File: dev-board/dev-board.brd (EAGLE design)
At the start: 49.2 x 64.8 mm, 43 parts, among them J1 12401832E402A, U1 STM32F103RET6, U2 AT24C64BN-10SU-2.7, U3 FT232RL, U4 MCP2551, U5 LM1117IMP-3.3, X1 8MHz

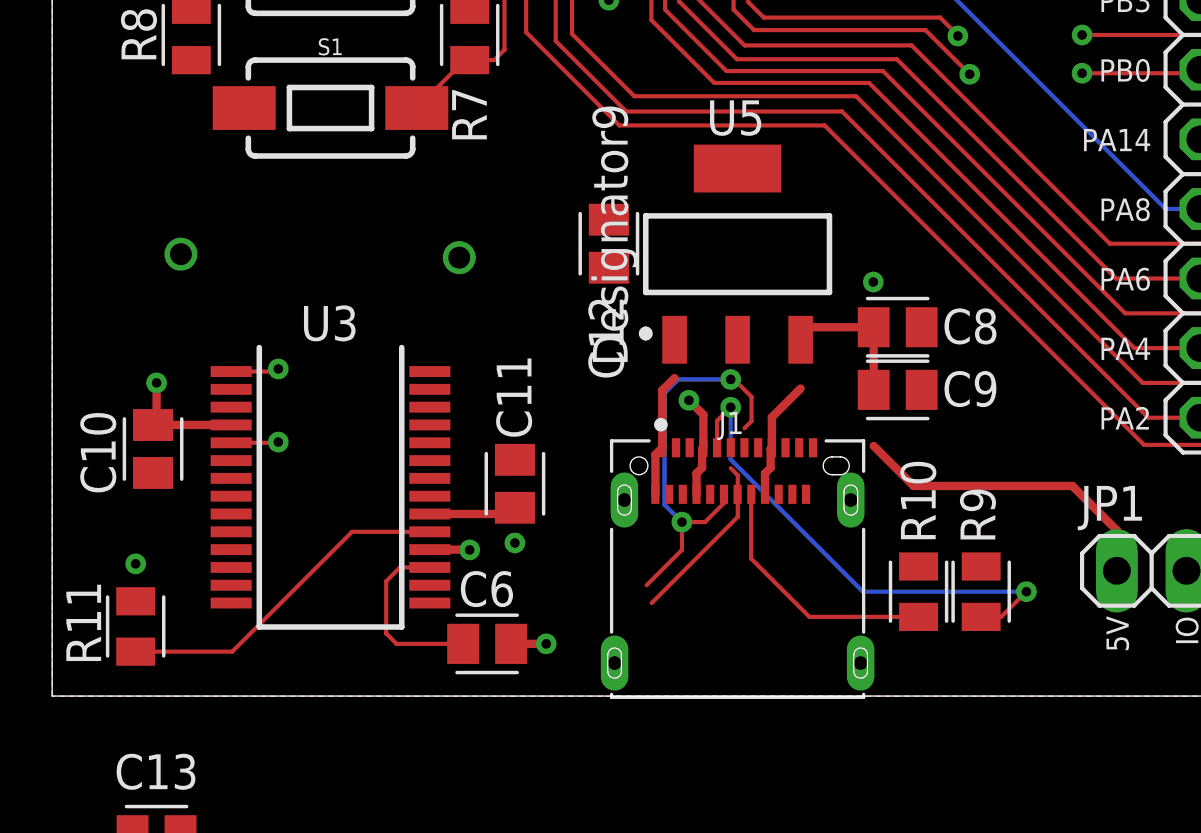
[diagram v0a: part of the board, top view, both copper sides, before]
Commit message: Redesign of dev-board USB connector area
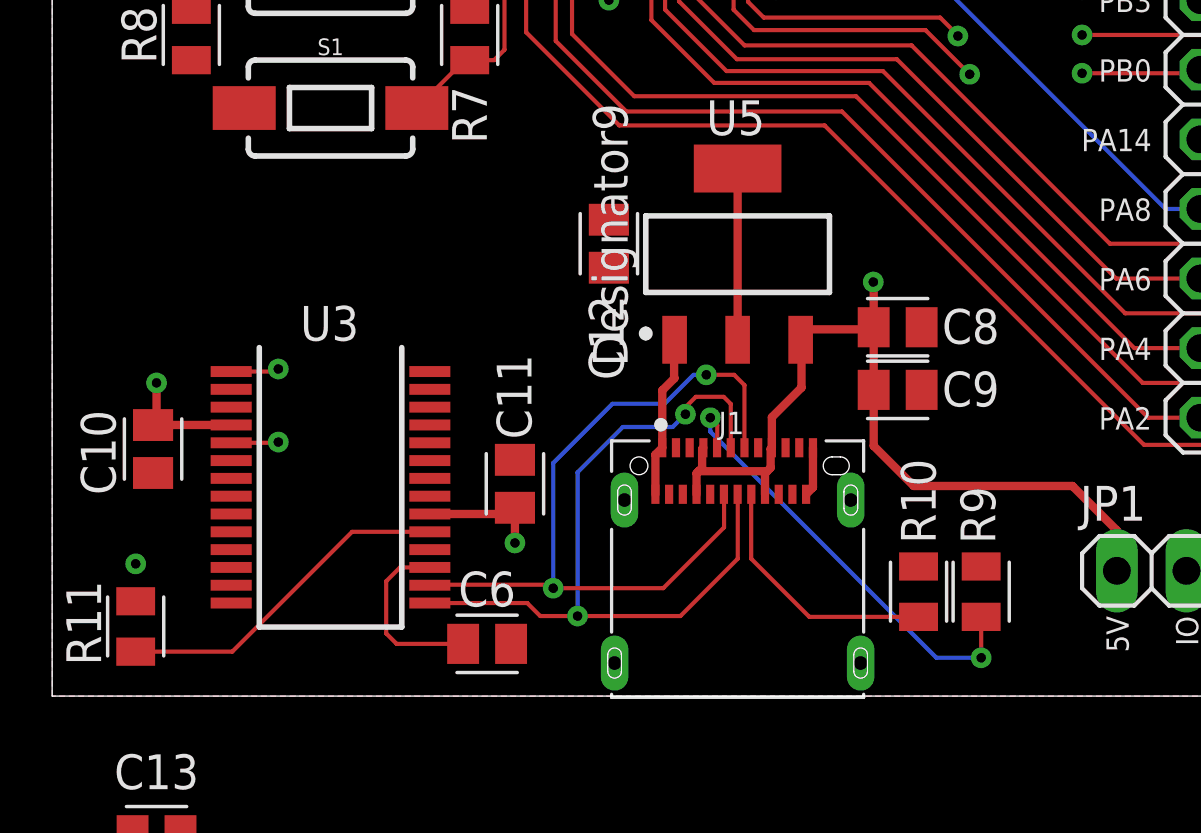
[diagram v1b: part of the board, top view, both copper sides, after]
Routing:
- net USBDP: track 6.34 -> 28.5 mm, vias 0 -> 2
- net USBDM: track 14.8 -> 28.3 mm
- net +5V: track 110.4 -> 117.6 mm, vias 5 -> 4
- net +3V3: track 24.7 -> 31.0 mm
- net N$13: track 18.4 -> 16.5 mm
- net GND: track 9.12 -> 9.60 mm, vias 8 -> 4

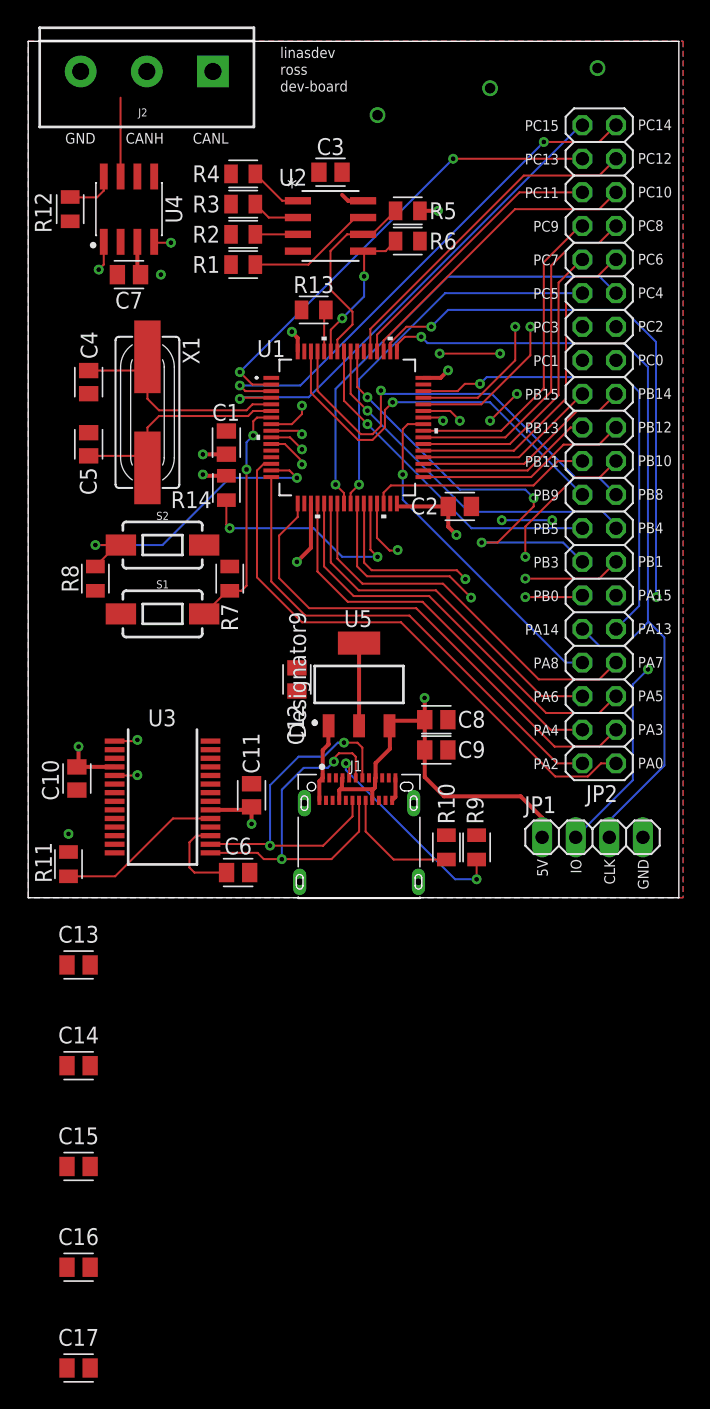
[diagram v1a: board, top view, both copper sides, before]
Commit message: Fix stm32 decoupling caps in dev-board pcb design
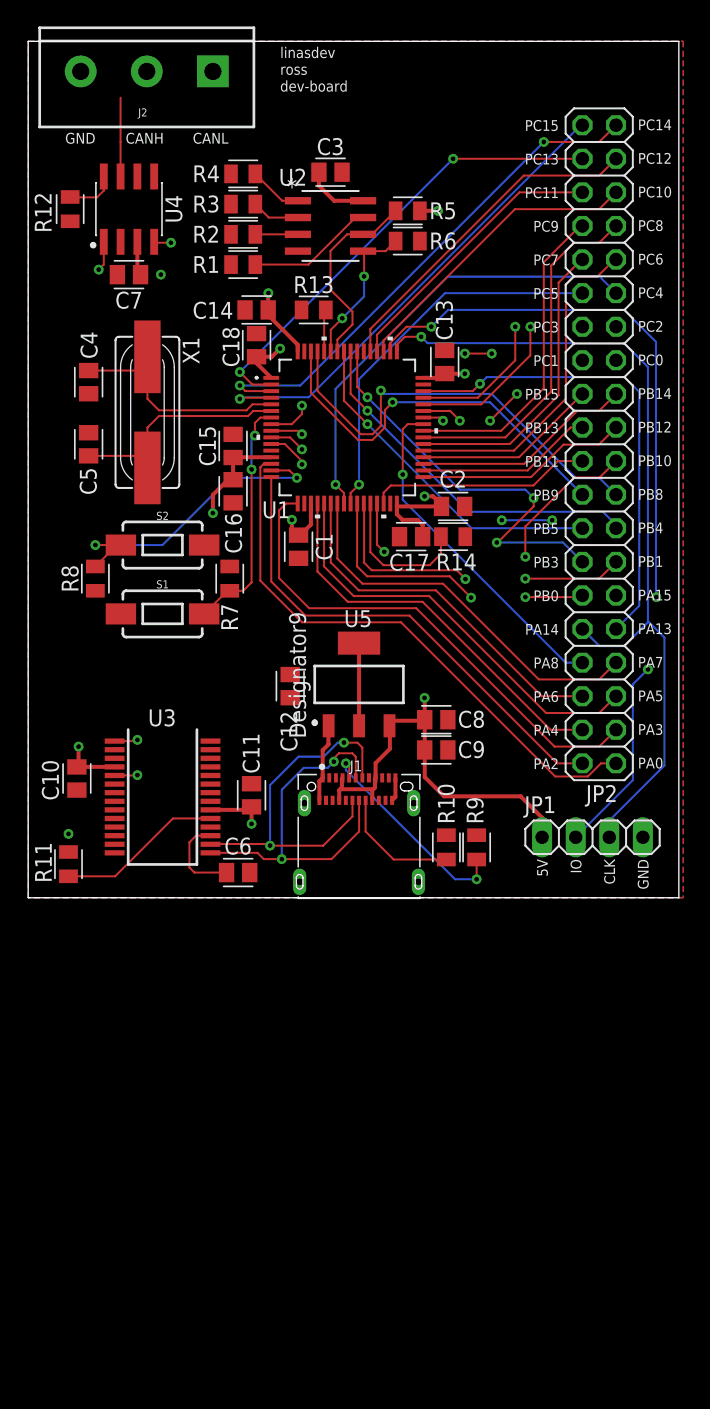
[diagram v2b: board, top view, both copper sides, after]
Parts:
- added C18: 100nF, Capacitor:CAPC2012X110
- moved C17 67.7 mm to (26.4, 27.3), turned to 180 degrees
- moved C16 59.8 mm to (13.0, 30.7), turned to 270 degrees
- moved C14 58.7 mm to (14.7, 44.5), turned to 180 degrees
- moved C15 55.7 mm to (13.0, 34.2), turned to 90 degrees
- moved C13 53.3 mm to (29.0, 40.5), turned to 90 degrees
- moved R14 17.5 mm to (29.6, 27.3), turned to 180 degrees
- moved C1 9.58 mm to (17.9, 26.5), turned to 270 degrees
- moved C12 0.72 mm to (17.3, 16.0)
- moved C2 0.51 mm to (29.6, 29.6)
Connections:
- net +3V3: now also C18.1
- net GND: now also C18.2
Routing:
- net +3V3: track 31.0 -> 51.6 mm, vias 7 -> 8
- net N$6: track 18.6 -> 11.1 mm, vias 2 -> 0
- net PB3: track 33.4 -> 31.2 mm
- net GND: track 9.60 -> 7.78 mm, vias 4 -> 0
- net PA3: track 37.5 -> 38.0 mm

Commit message: Put C12 bulk cap closer to regulator and provide more stitching vias
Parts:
- moved C12 3.75 mm to (19.1, 19.3), turned to 180 degrees
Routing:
- net +3V3: track 51.6 -> 63.1 mm, vias 8 -> 11
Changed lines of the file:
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@@
 <attribute name="VOLTAGE_RATING" value="" x="52.451" y="36.957" size="1.778" layer="27" rot="R90" display="off"/>
 </element>
-<element name="C12" library="Capacitor" library_urn="urn:adsk.eagle:library:16290819" package="CAPC2012X110" package3d_urn="urn:adsk.eagle:package:16290897/2" value="10uF" x="17.272" y="16.002" smashed="yes" rot="R270">
-<attribute name="CATEGORY" value="Capacitor" x="-20.828" y="-19.558" size="1.778" layer="27" rot="R270" display="off"/>
-<attribute name="MANUFACTURER" value="" x="-20.828" y="-19.558" size="1.778" layer="27" rot="R270" display="off"/>
-<attribute name="MPN" value="" x="-20.828" y="-19.558" size="1.778" layer="27" rot="R270" display="off"/>
-<attribute name="NAME" x="17.8107" y="12.573" size="1.27" layer="25" rot="R90" align="bottom-center"/>
-<attribute name="OPERATING_TEMP" value="" x="-20.828" y="-19.558" size="1.778" layer="27" rot="R270" display="off"/>
-<attribute name="PART_STATUS" value="" x="-20.828" y="-19.558" size="1.778" layer="27" rot="R270" display="off"/>
-<attribute name="ROHS_COMPLIANT" value="" x="-20.828" y="-19.558" size="1.778" layer="27" rot="R270" display="off"/>
-<attribute name="SERIES" value="" x="-20.828" y="-19.558" size="1.778" layer="27" rot="R270" display="off"/>
-<attribute name="SUB-CATEGORY" value="" x="-20.828" y="-19.558" size="1.778" layer="27" rot="R270" display="off"/>
-<attribute name="THERMALLOSS" value="" x="-20.828" y="-19.558" size="1.778" layer="27" rot="R270" display="off"/>
-<attribute name="TYPE" value="" x="-20.828" y="-19.558" size="1.778" layer="27" rot="R270" display="off"/>
-<attribute name="VOLTAGE_RATING" value="" x="-20.828" y="-19.558" size="1.778" layer="27" rot="R270" display="off"/>
+<element name="C12" library="Capacitor" library_urn="urn:adsk.eagle:library:16290819" package="CAPC2012X110" package3d_urn="urn:adsk.eagle:package:16290897/2" value="10uF" x="19.05" y="19.304" smashed="yes" rot="R180">
+<attribute name="CATEGORY" value="Capacitor" x="-16.51" y="57.404" size="1.778" layer="27" rot="R180" display="off"/>
+<attribute name="MANUFACTURER" value="" x="-16.51" y="57.404" size="1.778" layer="27" rot="R180" display="off"/>
+<attribute name="MPN" value="" x="-16.51" y="57.404" size="1.778" layer="27" rot="R180" display="off"/>
+<attribute name="NAME" x="19.05" y="20.6703" size="1.27" layer="25" align="bottom-center"/>
+<attribute name="OPERATING_TEMP" value="" x="-16.51" y="57.404" size="1.778" layer="27" rot="R180" display="off"/>
+<attribute name="PART_STATUS" value="" x="-16.51" y="57.404" size="1.778" layer="27" rot="R180" display="off"/>
+<attribute name="ROHS_COMPLIANT" value="" x="-16.51" y="57.404" size="1.778" layer="27" rot="R180" display="off"/>
+<attribute name="SERIES" value="" x="-16.51" y="57.404" size="1.778" layer="27" rot="R180" display="off"/>
+<attribute name="SUB-CATEGORY" value="" x="-16.51" y="57.404" size="1.778" layer="27" rot="R180" display="off"/>
+<attribute name="THERMALLOSS" value="" x="-16.51" y="57.404" size="1.778" layer="27" rot="R180" display="off"/>
+<attribute name="TYPE" value="" x="-16.51" y="57.404" size="1.778" layer="27" rot="R180" display="off"/>
+<attribute name="VOLTAGE_RATING" value="" x="-16.51" y="57.404" size="1.778" layer="27" rot="R180" display="off"/>
 </element>
 <element name="C2" library="Capacitor" library_urn="urn:adsk.eagle:library:16290819" package="CAPC2012X110" package3d_urn="urn:adsk.eagle:package:16290897/2" value="100nF" x="29.591" y="29.591" smashed="yes">
@@
 <attribute name="MANUFACTURER" value="" x="12.954" y="34.163" size="1.778" layer="27" rot="R90" display="off"/>
 <attribute name="MPN" value="" x="12.954" y="34.163" size="1.778" layer="27" rot="R90" display="off"/>
-<attribute name="NAME" x="11.6533" y="34.163" size="1.27" layer="25" rot="R90" align="bottom-center"/>
+<attribute name="NAME" x="13.0503" y="37.338" size="1.27" layer="25" rot="R90" align="bottom-center"/>
 <attribute name="OPERATING_TEMP" value="" x="12.954" y="34.163" size="1.778" layer="27" rot="R90" display="off"/>
 <attribute name="PART_STATUS" value="" x="12.954" y="34.163" size="1.778" layer="27" rot="R90" display="off"/>
@@
 <wire x1="28.956" y1="39.6376" x2="28.9696" y2="39.624" width="0.3048" layer="1"/>
 <wire x1="28.9696" y1="39.624" x2="30.48" y2="39.624" width="0.3048" layer="1"/>
+<wire x1="19.9254" y1="19.304" x2="22.429" y2="19.304" width="0.3048" layer="1"/>
+<wire x1="22.429" y1="19.304" x2="22.479" y2="19.254" width="0.3048" layer="1"/>
+<wire x1="22.479" y1="19.254" x2="23.191" y2="19.254" width="0.3048" layer="1"/>
+<wire x1="24.892" y1="19.939" x2="23.876" y2="19.939" width="0.3048" layer="1"/>
+<wire x1="23.876" y1="19.939" x2="23.191" y2="19.254" width="0.3048" layer="1"/>
+<via x="24.892" y="19.939" extent="1-16" drill="0.35"/>
+<wire x1="25.527" y1="19.304" x2="25.477" y2="19.254" width="0.3048" layer="1"/>
+<via x="25.527" y="19.304" extent="1-16" drill="0.35"/>
+<wire x1="22.479" y1="19.254" x2="22.783" y2="19.254" width="0.3048" layer="1"/>
+<wire x1="23.368" y1="18.669" x2="26.162" y2="18.669" width="0.3048" layer="1"/>
+<wire x1="23.368" y1="18.669" x2="22.783" y2="19.254" width="0.3048" layer="1"/>
+<via x="26.162" y="18.669" extent="1-16" drill="0.35"/>
+<wire x1="25.477" y1="19.254" x2="23.191" y2="19.254" width="0.3048" layer="1"/>
 <wire x1="27.0815" y1="49.657" x2="27.0815" y2="51.943" width="0" layer="19" extent="1-1"/>
 <wire x1="22.785" y1="52.705" x2="27.0815" y2="51.943" width="0" layer="19" extent="1-1"/>
@@
 <wire x1="18.84" y1="29.81" x2="15.84" y2="33.31" width="0" layer="19" extent="1-1"/>
 <wire x1="25.34" y1="29.81" x2="18.84" y2="29.81" width="0" layer="19" extent="1-1"/>
+<wire x1="24.892" y1="19.939" x2="27.2914" y2="27.305" width="0" layer="19" extent="1-1"/>
 <wire x1="27.34" y1="39.31" x2="27.432" y2="30.353" width="0" layer="19" extent="1-1"/>
-<wire x1="22.479" y1="19.254" x2="17.907" y2="27.4184" width="0" layer="19" extent="1-1"/>
-<wire x1="17.272" y1="16.8774" x2="22.479" y2="19.254" width="0" layer="19" extent="1-1"/>
-<wire x1="3.995" y1="9.895" x2="17.272" y2="16.8774" width="0" layer="19" extent="1-1"/>
+<wire x1="3.995" y1="9.895" x2="12.3905" y2="25.0495" width="0" layer="19" extent="1-1"/>
 </signal>
 <signal name="N$1">
@@
 <wire x1="30.5105" y1="27.305" x2="25.5406" y2="27.305" width="0" layer="19" extent="1-1"/>
 <wire x1="30.4664" y1="29.591" x2="30.5105" y2="27.305" width="0" layer="19" extent="1-1"/>
-<wire x1="4.445" y1="49.6007" x2="12.7965" y2="50.165" width="0" layer="19" extent="1-1"/>
-<wire x1="4.2046" y1="47.117" x2="4.445" y2="49.6007" width="0" layer="19" extent="1-1"/>
-<wire x1="0.635" y1="51.1505" x2="4.445" y2="49.6007" width="0" layer="19" extent="1-1"/>
-<wire x1="2.032" y1="38.1136" x2="4.2046" y2="47.117" width="0" layer="19" extent="1-1"/>
-<wire x1="2.032" y1="35.1654" x2="2.032" y2="38.1136" width="0" layer="19" extent="1-1"/>
-<wire x1="27.34" y1="38.81" x2="18.34" y2="41.31" width="0" layer="19" extent="1-1"/>
-<wire x1="28.956" y1="41.3884" x2="27.34" y2="38.81" width="0" layer="19" extent="1-1"/>
-<wire x1="17.272" y1="15.1266" x2="17.907" y2="25.6676" width="0" layer="19" extent="1-1"/>
-<wire x1="20.179" y1="13.004" x2="17.272" y2="15.1266" width="0" layer="19" extent="1-1"/>
+<wire x1="18.1746" y1="19.304" x2="17.907" y2="25.6676" width="0" layer="19" extent="1-1"/>
+<wire x1="20.179" y1="13.004" x2="18.1746" y2="19.304" width="0" layer="19" extent="1-1"/>
 <wire x1="18.349" y1="7.154" x2="19.479" y2="7.364" width="0" layer="19" extent="1-1"/>
 <wire x1="14.351" y1="8.6224" x2="18.349" y2="7.154" width="0" layer="19" extent="1-1"/>
@@
 <wire x1="3.995" y1="7.945" x2="11.245" y2="7.295" width="0" layer="19" extent="1-1"/>
 <wire x1="1.143" y1="8.1416" x2="3.995" y2="7.945" width="0" layer="19" extent="1-1"/>
+<wire x1="4.445" y1="49.6007" x2="12.7965" y2="50.165" width="0" layer="19" extent="1-1"/>
+<wire x1="4.2046" y1="47.117" x2="4.445" y2="49.6007" width="0" layer="19" extent="1-1"/>
+<wire x1="0.635" y1="51.1505" x2="4.445" y2="49.6007" width="0" layer="19" extent="1-1"/>
+<wire x1="2.032" y1="38.1136" x2="4.2046" y2="47.117" width="0" layer="19" extent="1-1"/>
+<wire x1="2.032" y1="35.1654" x2="2.032" y2="38.1136" width="0" layer="19" extent="1-1"/>
+<wire x1="27.34" y1="38.81" x2="18.34" y2="41.31" width="0" layer="19" extent="1-1"/>
+<wire x1="28.956" y1="41.3884" x2="27.34" y2="38.81" width="0" layer="19" extent="1-1"/>
 <wire x1="1.43" y1="62.484" x2="0.635" y2="51.1505" width="0" layer="19" extent="1-1"/>
 <wire x1="4.47" y1="21.463" x2="12.954" y2="29.8586" width="0" layer="19" extent="1-1"/>

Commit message: Move crystal oscillator closer to the stm32
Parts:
- moved C4 3.32 mm to (5.33, 38.6)
- moved C5 3.32 mm to (5.33, 34.7)
- moved X1 2.79 mm to (9.27, 36.7)
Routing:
- net OSC_IN: track 17.9 -> 14.6 mm
- net OSC_OUT: track 17.5 -> 14.7 mm
